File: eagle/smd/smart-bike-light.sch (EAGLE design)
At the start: 12 parts, among them IC1 LM2936MP-3.3, Q1 FDN360P, U1 ADXL362, U2 AL8805WS

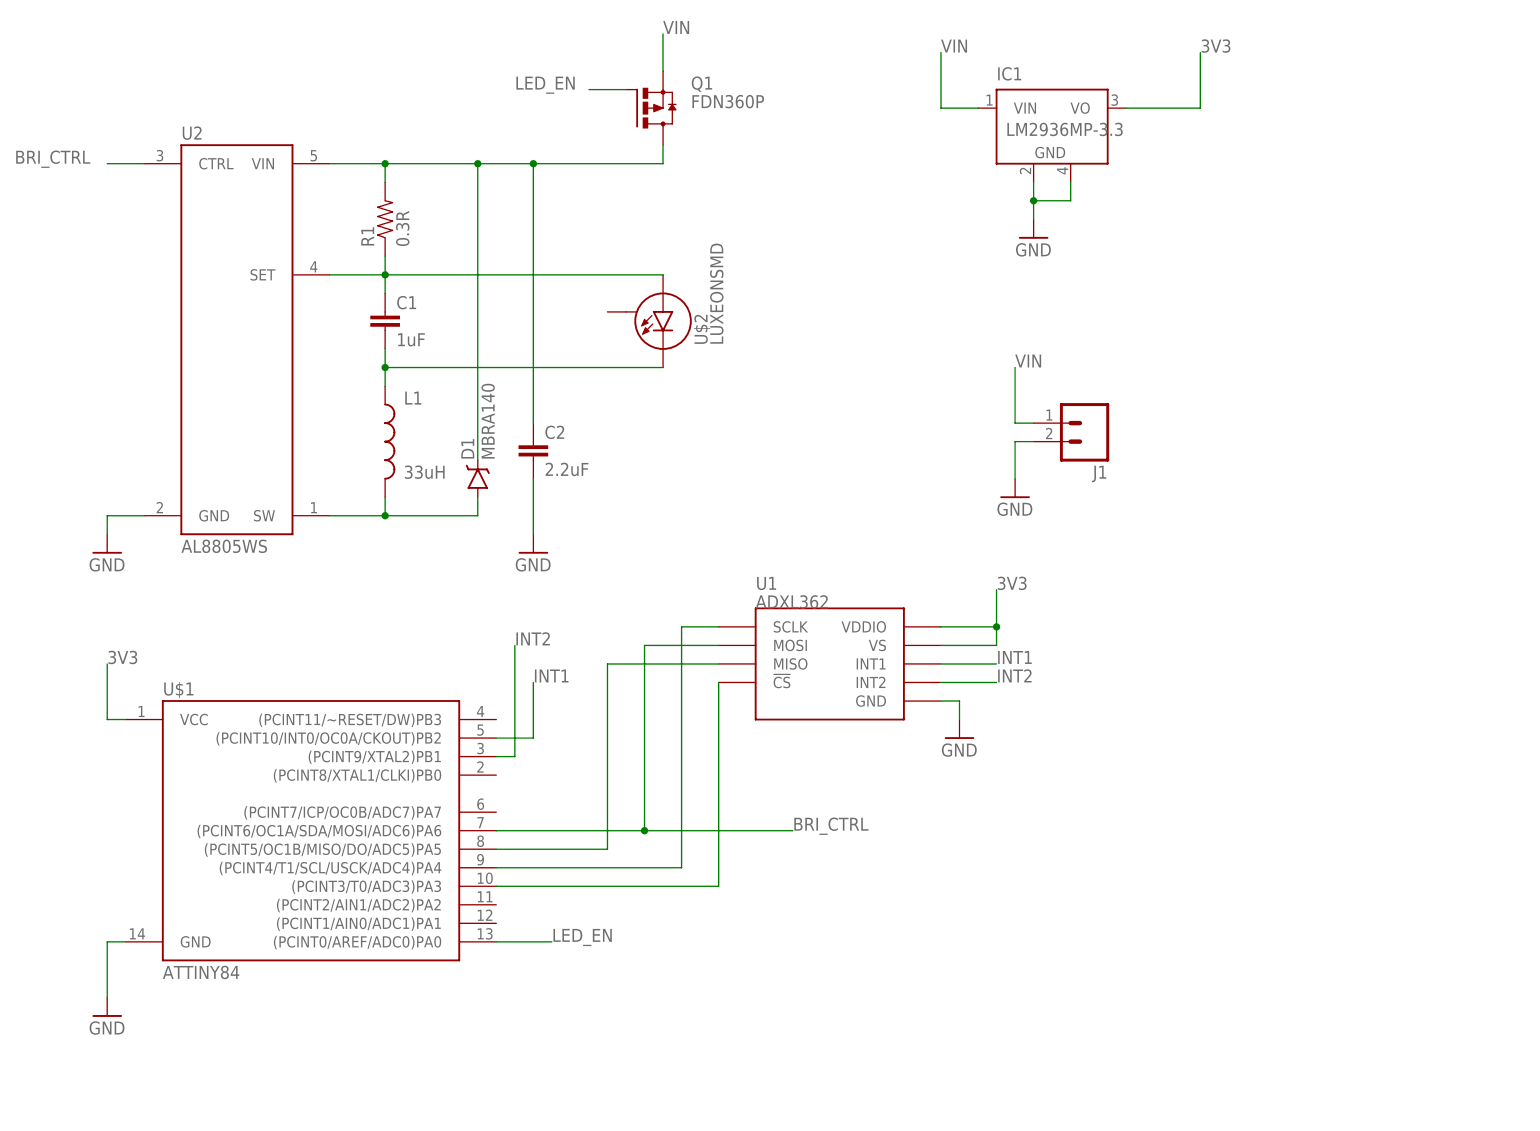
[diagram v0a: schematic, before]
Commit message: switched to analog accel
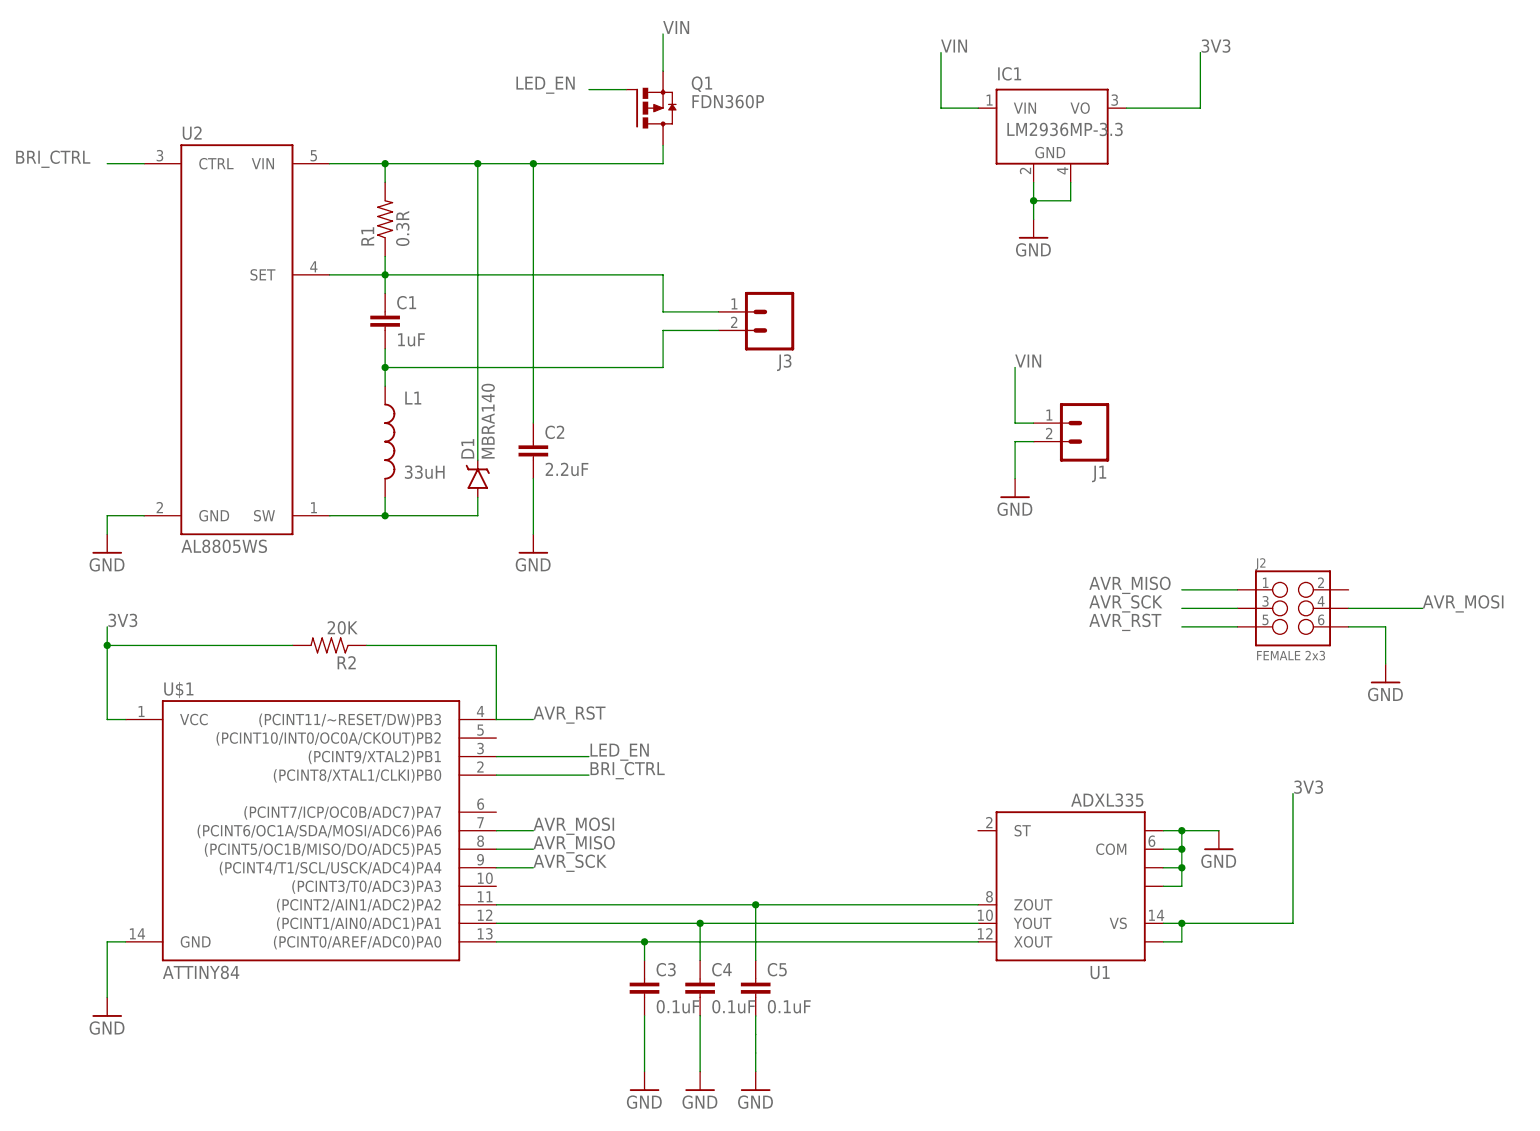
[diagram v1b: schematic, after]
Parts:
- removed U$2: LUXEONSMD, SparkFun-LED:LUXEONSMD
- added C3, C4, C5: 0.1uF, SparkFun-Capacitors:0.1UF-25V-5%(0603)
- added J2: FEMALE 2x3, SparkFun-Connectors:M03X2FEMALE
- added J3: (no value), SparkFun-Connectors:M02PTH
- added R2: 20K, SparkFun-Resistors:RESISTOR0603
- U1: value ADXL362 -> ADXL335; device SparkFun-Sensors:ADXL362 -> SparkFun-Sensors:ADXL335
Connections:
- removed net INT1: U$1.(PCINT10/INT0/OC0A/CKOUT)PB2, U1.INT1
- removed net INT2: U$1.(PCINT9/XTAL2)PB1, U1.INT2
- new net AVR_MISO: J2.1, U$1.(PCINT5/OC1B/MISO/DO/ADC5)PA5
- new net AVR_MOSI: J2.4, U$1.(PCINT6/OC1A/SDA/MOSI/ADC6)PA6
- new net AVR_RST: J2.5, R2.1, U$1.(PCINT11/~RESET/DW)PB3
- new net AVR_SCK: J2.3, U$1.(PCINT4/T1/SCL/USCK/ADC4)PA4
- net 3V3: now also R2.2, U1.VS@14, U1.VS@15; no longer U1.VDDIO, U1.VS
- net BRI_CTRL: now also U$1.(PCINT8/XTAL1/CLKI)PB0; no longer U$1.(PCINT6/OC1A/SDA/MOSI/ADC6)PA6, U1.MOSI
- net GND: now also C3.2, C4.2, C5.2, J2.6, U1.COM@3, U1.COM@5, U1.COM@6, U1.COM@7; no longer U1.GND
- net LED_EN: now also U$1.(PCINT9/XTAL2)PB1; no longer U$1.(PCINT0/AREF/ADC0)PA0
- net N$1: now also J3.1; no longer U$2.A
- net N$4: now also J3.2; no longer U$2.C
- net N$5: now also C3.1, U$1.(PCINT0/AREF/ADC0)PA0, U1.XOUT; no longer U$1.(PCINT5/OC1B/MISO/DO/ADC5)PA5, U1.MISO
- net N$6: now also C4.1, U$1.(PCINT1/AIN0/ADC1)PA1, U1.YOUT; no longer U$1.(PCINT4/T1/SCL/USCK/ADC4)PA4, U1.SCLK
- net N$7: now also C5.1, U$1.(PCINT2/AIN1/ADC2)PA2, U1.ZOUT; no longer U$1.(PCINT3/T0/ADC3)PA3, U1.!CS

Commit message: updated jumper silkscreens, README
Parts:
- renumbered J1 to POWER
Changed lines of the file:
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@@
 <part name="U$1" library="SparkFun-DigitalIC" deviceset="ATTINY84" device=""/>
 <part name="U2" library="SparkFun-PowerIC" deviceset="AL8805" device="" value="AL8805WS"/>
-<part name="J1" library="SparkFun-Connectors" deviceset="M02" device="PTH"/>
+<part name="POWER" library="SparkFun-Connectors" deviceset="M02" device="PTH"/>
 <part name="R1" library="SparkFun-Resistors" deviceset="RESISTOR" device="0603" value="0.3R"/>
 <part name="D1" library="SparkFun-DiscreteSemi" deviceset="MBRA140" device=""/>
@@
 <instance part="U$1" gate="G$1" x="53.34" y="38.1"/>
 <instance part="U2" gate="G$1" x="43.18" y="111.76"/>
-<instance part="J1" gate="G$1" x="160.02" y="93.98" rot="R180"/>
+<instance part="POWER" gate="G$1" x="160.02" y="93.98" rot="R180"/>
 <instance part="R1" gate="G$1" x="63.5" y="121.92" rot="R90"/>
 <instance part="D1" gate="G$1" x="76.2" y="86.36" rot="R90"/>
@@
 </segment>
 <segment>
-<pinref part="J1" gate="G$1" pin="2"/>
+<pinref part="POWER" gate="G$1" pin="2"/>
 <pinref part="GND3" gate="1" pin="GND"/>
 <wire x1="152.4" y1="91.44" x2="149.86" y2="91.44" width="0.1524" layer="91"/>
@@
 <net name="VIN" class="0">
 <segment>
-<pinref part="J1" gate="G$1" pin="1"/>
+<pinref part="POWER" gate="G$1" pin="1"/>
 <wire x1="152.4" y1="93.98" x2="149.86" y2="93.98" width="0.1524" layer="91"/>
 <wire x1="149.86" y1="93.98" x2="149.86" y2="101.6" width="0.1524" layer="91"/>
